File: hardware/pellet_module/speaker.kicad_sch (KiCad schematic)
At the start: 15 parts, among them U3 TPA2005D1

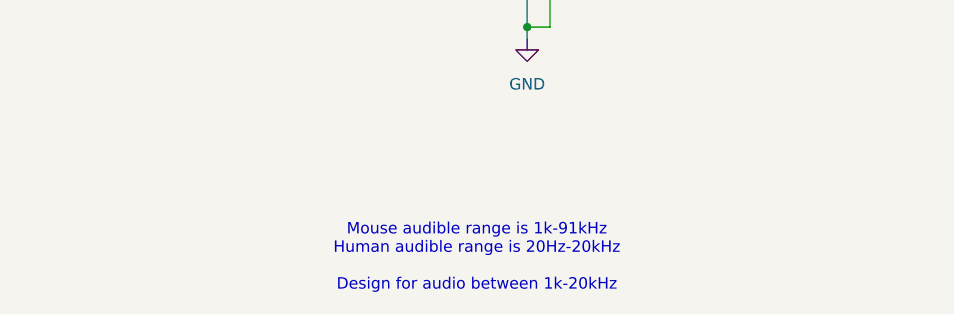
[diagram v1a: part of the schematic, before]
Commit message: Fixes based on discovered issues on testing rig
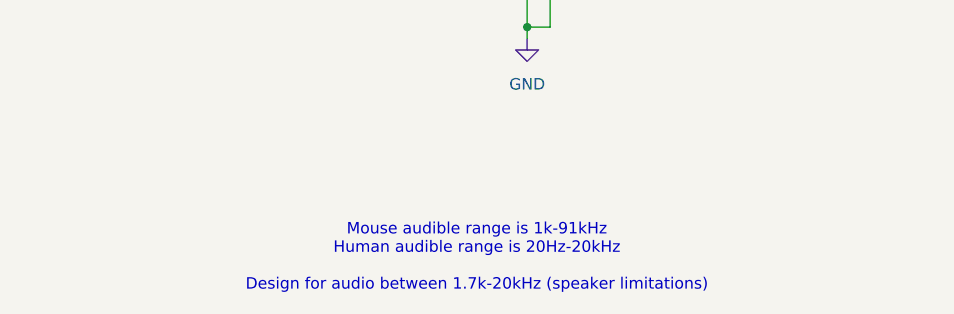
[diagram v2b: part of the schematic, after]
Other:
- note added: "Mouse audible range is 1k-91kHz Human audible range is 20Hz-20kHz Design for audio between 1.7k-20kHz (speaker limitations)"
- note removed: "Mouse audible range is 1k-91kHz Human audible range is 20Hz-20kHz Design for audio between 1k-20kHz"
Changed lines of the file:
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@@
 		)
 	)
-	(text "Mouse audible range is 1k-91kHz\nHuman audible range is 20Hz-20kHz\n\nDesign for audio between 1k-20kHz"
+	(text "Mouse audible range is 1k-91kHz\nHuman audible range is 20Hz-20kHz\n\nDesign for audio between 1.7k-20kHz (speaker limitations)"
 		(exclude_from_sim no)
 		(at 150.622 133.604 0)

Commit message: Update Pellet BOM for part availability
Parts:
- C14, C15: LCSC C162235 -> C107051
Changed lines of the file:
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@@
 			)
 		)
-		(property "LCSC" "C162235"
+		(property "LCSC" "C107051"
 			(at 74.93 90.17 0)
 			(effects
@@
 			)
 		)
-		(property "LCSC" "C162235"
+		(property "LCSC" "C107051"
 			(at 74.93 100.33 0)
 			(effects
